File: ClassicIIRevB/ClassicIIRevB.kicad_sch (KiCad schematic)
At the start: 57 parts, among them J11 POWER/ANALOG, J15 BURN-IN

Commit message: Show smaller ROM footprints
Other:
- sheet Expansion Slot renamed Expansion Slot and Jumpers
- sheet System ROM renamed System ROM 128K & 256K
- added sheet System ROM 512K & 1M (rom2.kicad_sch)
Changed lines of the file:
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@@
 	(title_block
 		(title "Macintosh Classic II Revision B")
-		(date "2025-05-29")
+		(date "2025-05-31")
 		(company "Apple Computer")
 		(comment 1 "drawn by Bradley Bell")
@@
 	)
 	(sheet
-		(at 127 25.4)
+		(at 114.3 25.4)
 		(size 12.7 3.81)
 		(exclude_from_sim no)
@@
 		)
 		(property "Sheetname" "ADB & Battery"
-			(at 127 24.6884 0)
+			(at 114.3 24.6884 0)
 			(effects
 				(font
@@
 		)
 		(property "Sheetfile" "egret.kicad_sch"
-			(at 127 29.7946 0)
+			(at 114.3 29.7946 0)
 			(effects
 				(font
@@
 	)
 	(sheet
-		(at 203.2 35.56)
+		(at 139.7 45.72)
+		(size 12.7 3.81)
+		(exclude_from_sim no)
+		(in_bom yes)
+		(on_board yes)
+		(dnp no)
+		(fields_autoplaced yes)
+		(stroke
+			(width 0.1524)
+			(type solid)
+		)
+		(fill
+			(color 0 0 0 0.0000)
+		)
+		(property "Sheetname" "System ROM 512K & 1M"
+			(at 139.7 45.0084 0)
+			(effects
+				(font
+					(size 1.27 1.27)
+				)
+				(justify left bottom)
+			)
+		)
+		(property "Sheetfile" "rom2.kicad_sch"
+			(at 139.7 50.1146 0)
+			(effects
+				(font
+					(size 1.27 1.27)
+				)
+				(justify left top)
+			)
+		)
+		(instances
+			(project "ClassicIIRevB"
+				(path "/08c23af6-72f1-4a8f-a60c-b986fe71300f"
+					(page "7")
+				)
+			)
+		)
+	)
+	(sheet
+		(at 201.93 45.72)
 		(size 12.7 3.81)
 		(exclude_from_sim no)
@@
 		)
 		(property "Sheetname" "Floppy"
-			(at 203.2 34.8484 0)
+			(at 201.93 45.0084 0)
 			(effects
 				(font
@@
 		)
 		(property "Sheetfile" "floppy.kicad_sch"
-			(at 203.2 39.9546 0)
+			(at 201.93 50.1146 0)
 			(effects
 				(font
@@
 			(project "ClassicIIRevB"
 				(path "/08c23af6-72f1-4a8f-a60c-b986fe71300f"
-					(page "12")
+					(page "13")
 				)
 			)
@@
 	)
 	(sheet
-		(at 177.8 35.56)
+		(at 177.8 45.72)
 		(size 12.7 3.81)
 		(exclude_from_sim no)
@@
 		)
 		(property "Sheetname" "RAM Expansion"
-			(at 177.8 34.8484 0)
+			(at 177.8 45.0084 0)
 			(effects
 				(font
@@
 		)
 		(property "Sheetfile" "simm.kicad_sch"
-			(at 177.8 39.9546 0)
+			(at 177.8 50.1146 0)
 			(effects
 				(font
@@
 			(project "ClassicIIRevB"
 				(path "/08c23af6-72f1-4a8f-a60c-b986fe71300f"
-					(page "9")
+					(page "10")
 				)
 			)
@@
 	)
 	(sheet
-		(at 177.8 45.72)
+		(at 201.93 25.4)
 		(size 12.7 3.81)
 		(exclude_from_sim no)
@@
 		)
 		(property "Sheetname" "SCSI & Serial"
-			(at 177.8 45.0084 0)
+			(at 201.93 24.6884 0)
 			(effects
 				(font
@@
 		)
 		(property "Sheetfile" "scsi.kicad_sch"
-			(at 177.8 50.1146 0)
+			(at 201.93 29.7946 0)
 			(effects
 				(font
@@
 			(project "ClassicIIRevB"
 				(path "/08c23af6-72f1-4a8f-a60c-b986fe71300f"
-					(page "10")
+					(page "11")
 				)
 			)
@@
 	)
 	(sheet
-		(at 177.8 25.4)
+		(at 177.8 35.56)
 		(size 12.7 3.81)
 		(exclude_from_sim no)
@@
 		)
 		(property "Sheetname" "RAM"
-			(at 177.8 24.6884 0)
+			(at 177.8 34.8484 0)
 			(effects
 				(font
@@
 		)
 		(property "Sheetfile" "ram.kicad_sch"
-			(at 177.8 29.7946 0)
+			(at 177.8 39.9546 0)
 			(effects
 				(font
@@
 			(project "ClassicIIRevB"
 				(path "/08c23af6-72f1-4a8f-a60c-b986fe71300f"
-					(page "8")
+					(page "9")
 				)
 			)
@@
 	)
 	(sheet
-		(at 152.4 45.72)
+		(at 177.8 25.4)
 		(size 12.7 3.81)
 		(exclude_from_sim no)
@@
 		)
 		(property "Sheetname" "RAM Transceivers"
-			(at 152.4 45.0084 0)
+			(at 177.8 24.6884 0)
 			(effects
 				(font
@@
 		)
 		(property "Sheetfile" "xcvr.kicad_sch"
-			(at 152.4 50.1146 0)
+			(at 177.8 29.7946 0)
 			(effects
 				(font
@@
 			(project "ClassicIIRevB"
 				(path "/08c23af6-72f1-4a8f-a60c-b986fe71300f"
-					(page "7")
+					(page "8")
 				)
 			)
@@
 	)
 	(sheet
-		(at 127 45.72)
+		(at 114.3 45.72)
 		(size 12.7 3.81)
 		(exclude_from_sim no)
@@
 		)
 		(property "Sheetname" "EAGLE"
-			(at 127 45.0084 0)
+			(at 114.3 45.0084 0)
 			(effects
 				(font
@@
 		)
 		(property "Sheetfile" "eagle.kicad_sch"
-			(at 127 50.1146 0)
+			(at 114.3 50.1146 0)
 			(effects
 				(font
@@
 	)
 	(sheet
-		(at 152.4 35.56)
+		(at 139.7 25.4)
 		(size 12.7 3.81)
 		(exclude_from_sim no)
@@
 			(color 0 0 0 0.0000)
 		)
-		(property "Sheetname" "Expansion Slot"
-			(at 152.4 34.8484 0)
+		(property "Sheetname" "Expansion Slot and Jumpers"
+			(at 139.7 24.6884 0)
 			(effects
 				(font
@@
 		)
 		(property "Sheetfile" "romfpu.kicad_sch"
-			(at 152.4 39.9546 0)
+			(at 139.7 29.7946 0)
 			(effects
 				(font
@@
 			(project "ClassicIIRevB"
 				(path "/08c23af6-72f1-4a8f-a60c-b986fe71300f"
-					(page "6")
+					(page "5")
 				)
 			)
@@
 	)
 	(sheet
-		(at 203.2 45.72)
+		(at 228.6 25.4)
 		(size 12.7 3.81)
 		(exclude_from_sim no)
@@
 		)
 		(property "Sheetname" "Sound"
-			(at 203.2 45.0084 0)
+			(at 228.6 24.6884 0)
 			(effects
 				(font
@@
 		)
 		(property "Sheetfile" "sound.kicad_sch"
-			(at 203.2 50.1146 0)
+			(at 228.6 29.7946 0)
 			(effects
 				(font
@@
 			(project "ClassicIIRevB"
 				(path "/08c23af6-72f1-4a8f-a60c-b986fe71300f"
-					(page "13")
+					(page "14")
 				)
 			)
@@
 	)
 	(sheet
-		(at 127 35.56)
+		(at 114.3 35.56)
 		(size 12.7 3.81)
 		(exclude_from_sim no)
@@
 		)
 		(property "Sheetname" "CPU"
-			(at 127 34.8484 0)
+			(at 114.3 34.8484 0)
 			(effects
 				(font
@@
 		)
 		(property "Sheetfile" "cpu.kicad_sch"
-			(at 127 39.9546 0)
+			(at 114.3 39.9546 0)
 			(effects
 				(font
@@
 	)
 	(sheet
-		(at 203.2 25.4)
+		(at 201.93 35.56)
 		(size 12.7 3.81)
 		(exclude_from_sim no)
@@
 		)
 		(property "Sheetname" "Serial"
-			(at 203.2 24.638 0)
+			(at 201.93 34.798 0)
 			(effects
 				(font
@@
 		)
 		(property "Sheetfile" "serial.kicad_sch"
-			(at 203.2 29.718 0)
+			(at 201.93 39.878 0)
 			(effects
 				(font
@@
 			(project "ClassicIIRevB"
 				(path "/08c23af6-72f1-4a8f-a60c-b986fe71300f"
-					(page "11")
+					(page "12")
 				)
 			)
@@
 	)
 	(sheet
-		(at 228.6 25.4)
+		(at 228.6 35.56)
 		(size 12.7 3.81)
 		(exclude_from_sim no)
@@
 		)
 		(property "Sheetname" "DFAC"
-			(at 228.6 24.6884 0)
+			(at 228.6 34.8484 0)
 			(effects
 				(font
@@
 		)
 		(property "Sheetfile" "dfac.kicad_sch"
-			(at 228.6 29.7946 0)
+			(at 228.6 39.9546 0)
 			(effects
 				(font
@@
 			(project "ClassicIIRevB"
 				(path "/08c23af6-72f1-4a8f-a60c-b986fe71300f"
-					(page "14")
+					(page "15")
 				)
 			)
@@
 	)
 	(sheet
-		(at 152.4 25.4)
+		(at 139.7 35.56)
 		(size 12.7 3.81)
 		(exclude_from_sim no)
@@
 			(color 0 0 0 0.0000)
 		)
-		(property "Sheetname" "System ROM"
-			(at 152.4 24.6884 0)
+		(property "Sheetname" "System ROM 128K & 256K"
+			(at 139.7 34.8484 0)
 			(effects
 				(font
@@
 		)
 		(property "Sheetfile" "rom.kicad_sch"
-			(at 152.4 29.7946 0)
+			(at 139.7 39.9546 0)
 			(effects
 				(font
@@
 			(project "ClassicIIRevB"
 				(path "/08c23af6-72f1-4a8f-a60c-b986fe71300f"
-					(page "5")
+					(page "6")
 				)
 			)
@@
 			(project "ClassicIIRevB"
 				(path "/08c23af6-72f1-4a8f-a60c-b986fe71300f"
-					(page "15")
+					(page "16")
 				)
 			)

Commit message: improved footprints and silkscreens
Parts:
- FD1, FD6: footprint Fiducial:Fiducial_1mm_Mask3mm -> MyPackage:Fiducial_1mm_Mask3mm_square
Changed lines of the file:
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@@
 	(title_block
 		(title "Macintosh Classic II Revision B")
-		(date "2025-05-31")
+		(date "2025-06-04")
 		(company "Apple Computer")
 		(comment 1 "drawn by Bradley Bell")
@@
 			)
 		)
-		(property "Footprint" "Fiducial:Fiducial_1mm_Mask3mm"
+		(property "Footprint" "MyPackage:Fiducial_1mm_Mask3mm_square"
 			(at 147.32 200.66 0)
 			(effects
@@
 			)
 		)
-		(property "Footprint" "Fiducial:Fiducial_1mm_Mask3mm"
+		(property "Footprint" "MyPackage:Fiducial_1mm_Mask3mm_square"
 			(at 147.32 175.26 0)
 			(effects

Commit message: Switch to some "official" net names
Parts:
- added R83: 100, MyPackage:SMD_0805_2012Metric_Pad1.25x1.65mm, symbol Device:R_Small_US
- added TP186: ~, MyPackage:TestPoint_THTPad_D1.0mm_Drill0.5mm, symbol Connector:TestPoint
- F1: value Polyfuse_Small -> 1A
- L10, L2: value L_Ferrite_Small -> Ferrite
- L7: value L_Ferrite_Small -> FERRITE
- renumbered alt_G1 to ZG1
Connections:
- net BURN7 renamed BURNIN
- net OSC_VCC renamed G1_5V
- net PBL renamed PWM
- net SCSI_BSY renamed BSY
- net SPEAKER renamed SNDPOS
- net SYSCLOCKIN renamed 32MC
- net VIDEO renamed VIDOUTF
- net VIDOUTF: now also R83.2, TP186.1
- new net VIDOUT: R83.1
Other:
- moved on the sheet: C26, C31, C90, F1, J15, L10, L2, R76, R85, R93, R95

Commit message: update exports
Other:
- title: Macintosh Classic II Revision B -> Macintosh Classic II (Later Revision)
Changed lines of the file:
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@@
 	(paper "USLetter")
 	(title_block
-		(title "Macintosh Classic II Revision B")
-		(date "2025-06-04")
+		(title "Macintosh Classic II (Later Revision)")
+		(date "2025-06-16")
 		(company "Apple Computer")
 		(comment 1 "drawn by Bradley Bell")

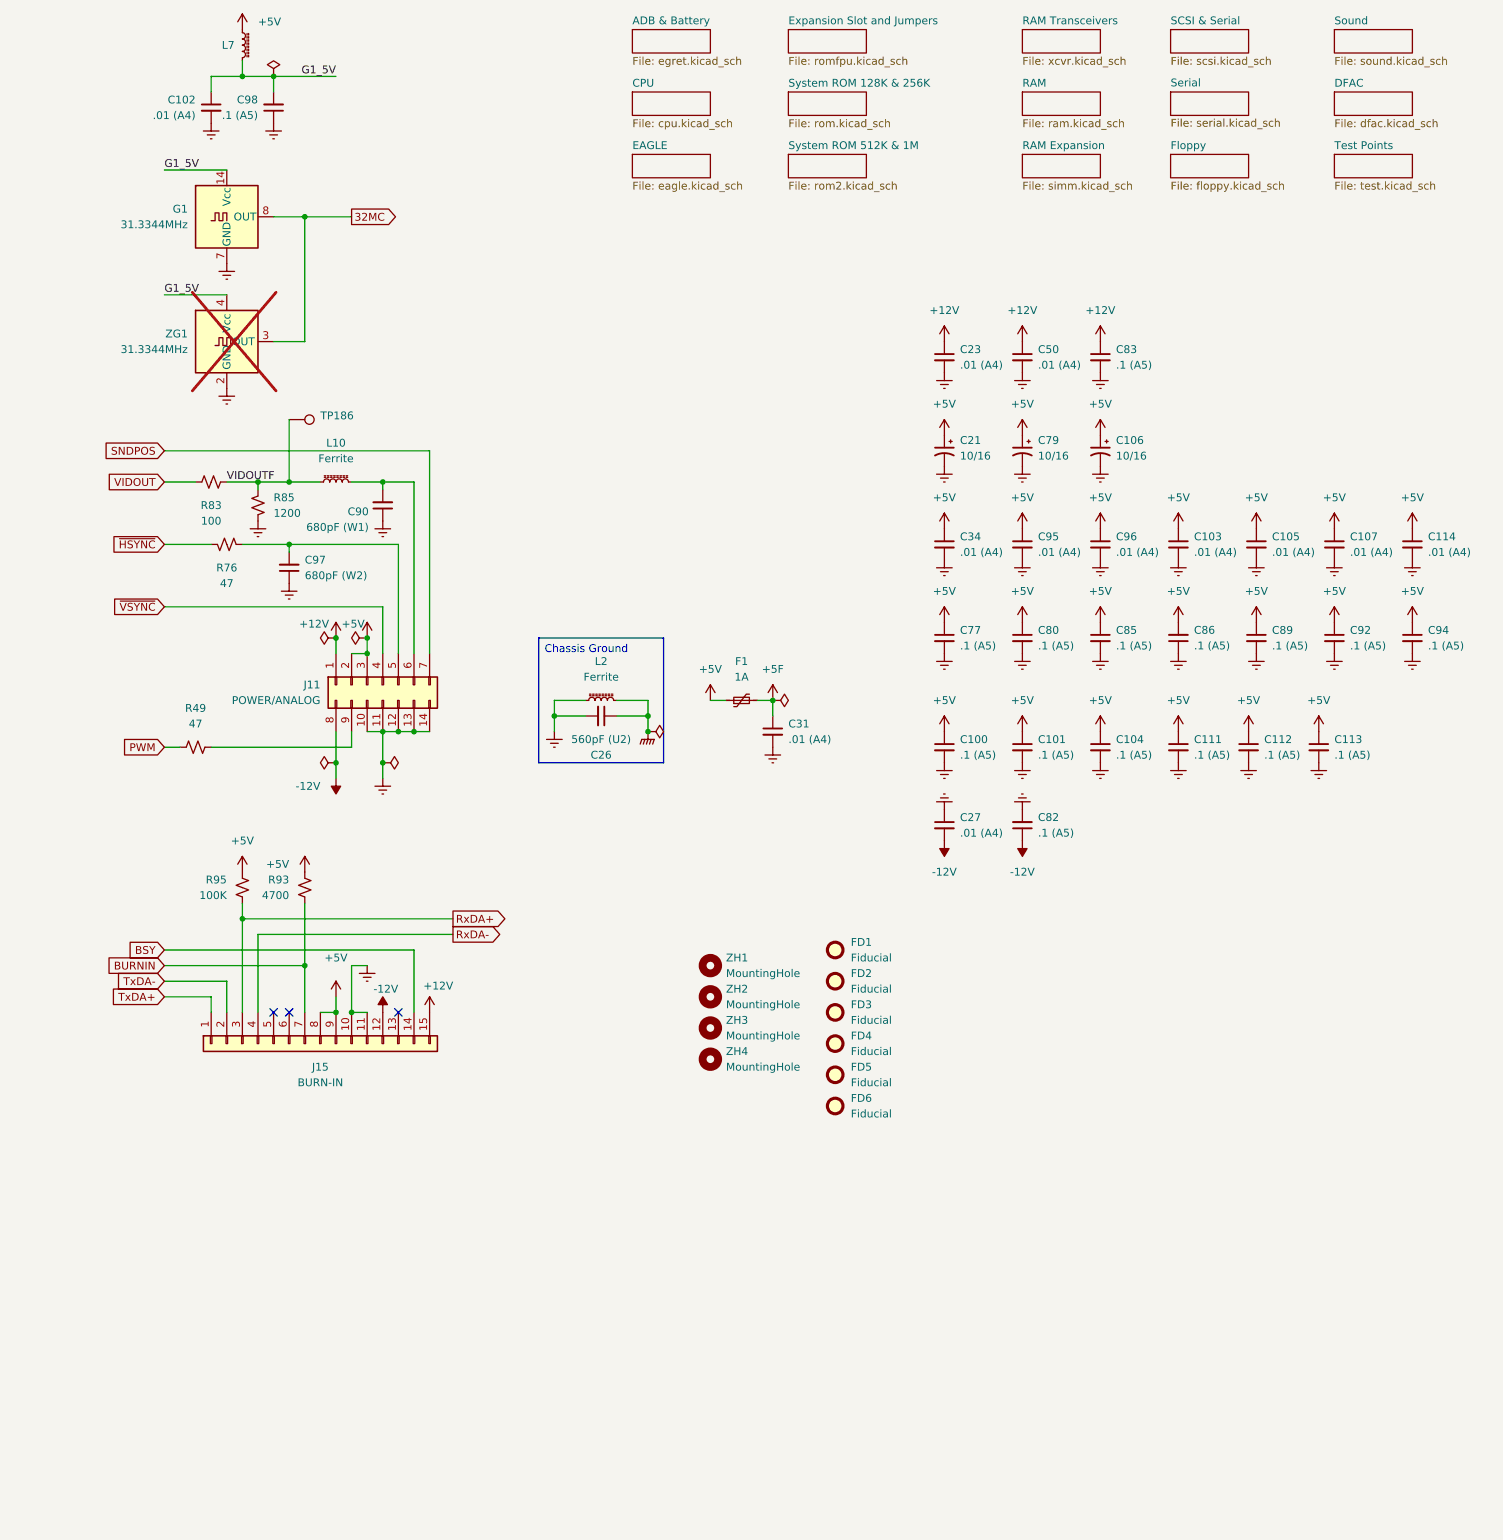
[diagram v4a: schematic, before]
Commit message: Corrections to SMDs, more improved footprints
The later revision board reproduction design is now complete.
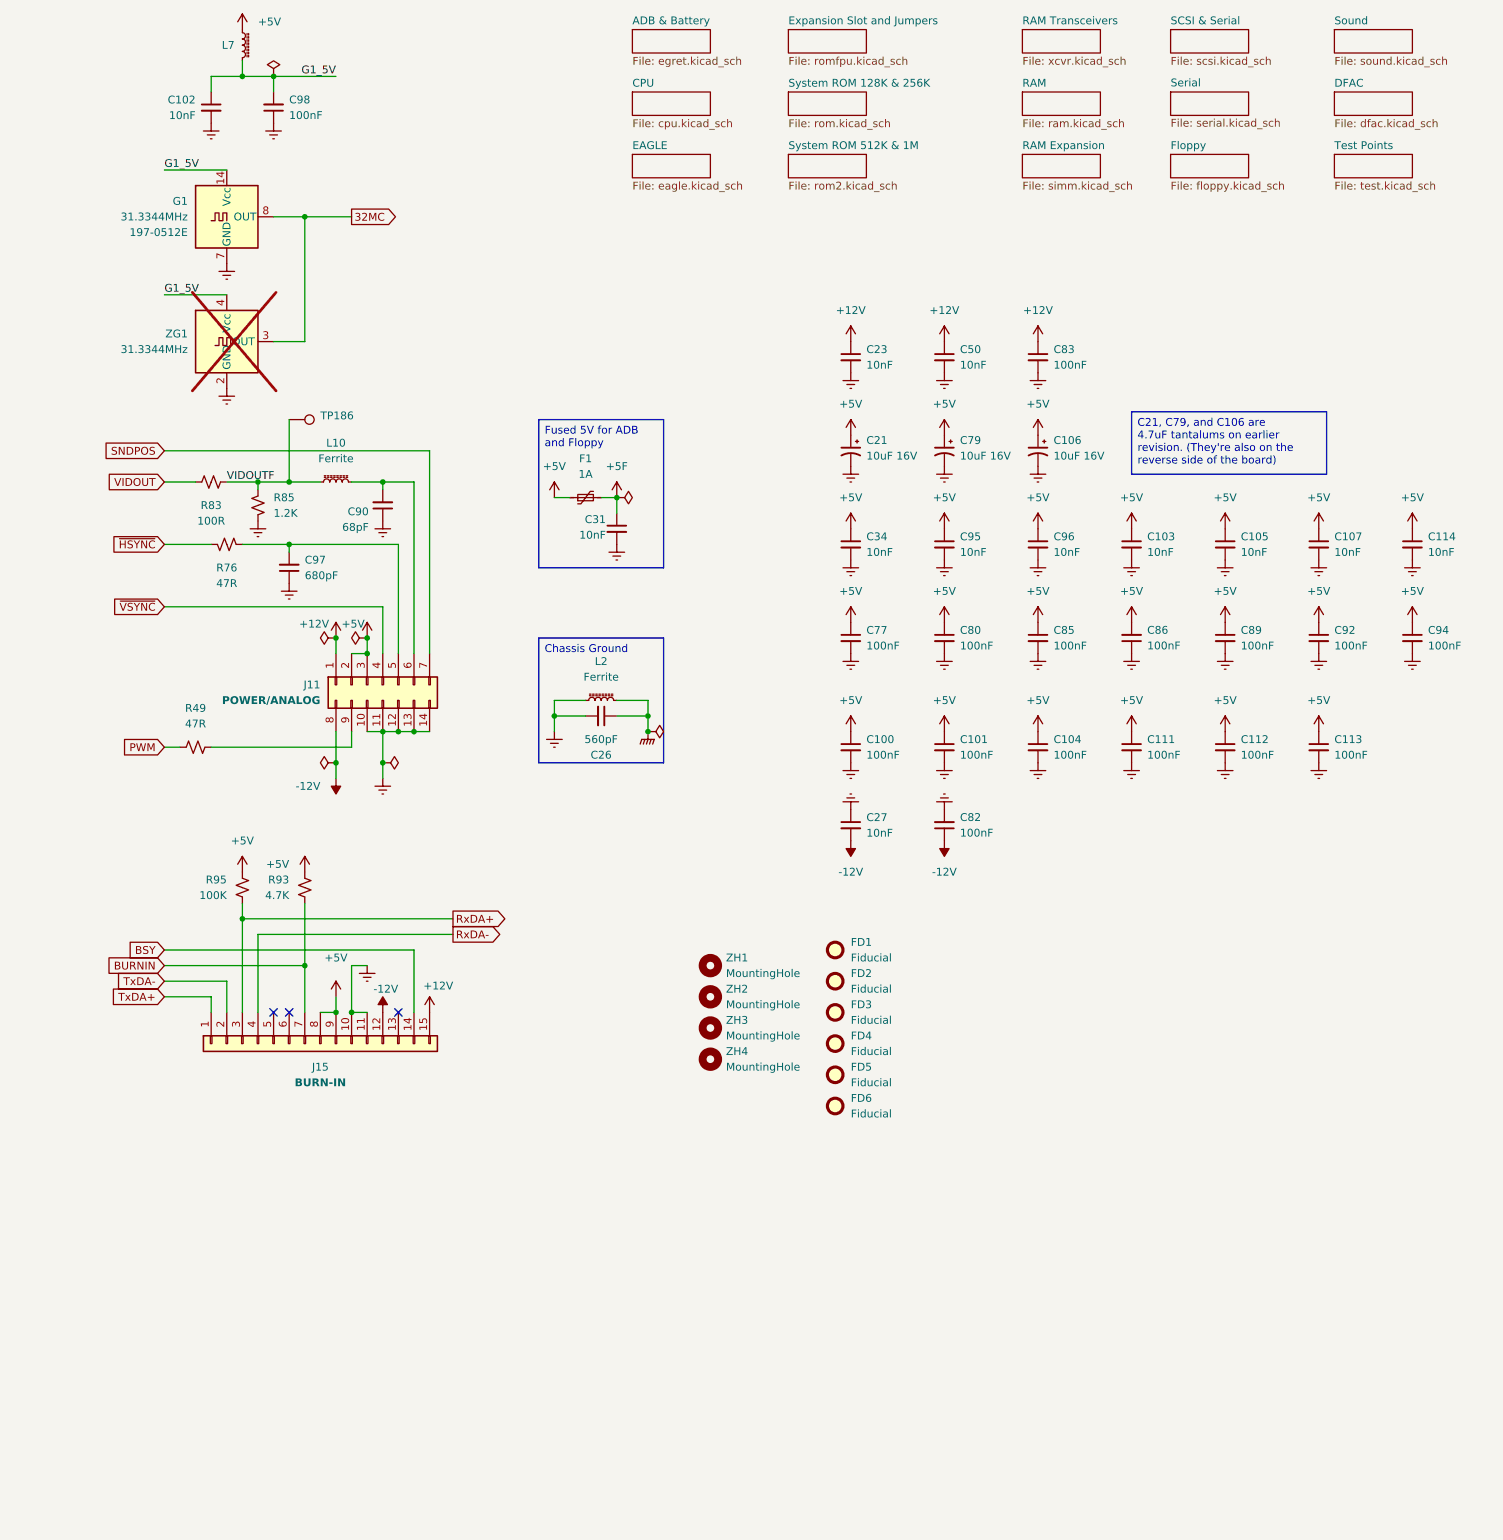
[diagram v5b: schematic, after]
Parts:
- C100, C101, C104, C111, C112, C113, C77, C80, C82, C83, C85, C86, C89, C92, C94, C98: value .1 (A5) -> 100nF
- C102, C103, C105, C107, C114, C23, C27, C31, C34, C50, C95, C96: value .01 (A4) -> 10nF
- C106, C79: value 10/16 -> 10uF 16V; Note (none) -> 4.7uF tant on earlier revision
- C21: value 10/16 -> 10uF 16V; Note (none) -> 4.7uF tant on early revision
- C26: value 560pF (U2) -> 560pF
- C90: value 680pF (W1) -> 68pF
- C97: value 680pF (W2) -> 680pF
- G1: footprint Oscillator:Oscillator_DIP-14 -> MyPackage:Oscillator_DIP-14; PartNum (none) -> 197-0512E
- J15, TP186: now left out of the parts list
- L7: value FERRITE -> Ferrite
- R49, R76: value 47 -> 47R
- R83: value 100 -> 100R
- R85: value 1200 -> 1.2K
- R93: value 4700 -> 4.7K
- ZG1: footprint Oscillator:Oscillator_SMD_Abracon_ABLNO -> MyPackage:Oscillator_SMD_Abracon_ABLNO
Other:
- moved on the sheet: C100, C101, C103, C104, C105, C106, C107, C111, C112, C21, C23, C27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

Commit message: Fix zones
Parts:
- ZH1, ZH2, ZH3, ZH4: footprint MountingHole:MountingHole_3.2mm_M3_ISO14580 -> MyPackage:MountingHole_3.2mm_M3_ISO14580
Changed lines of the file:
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@@
 	(title_block
 		(title "Macintosh Classic II (Later Revision)")
-		(date "2025-06-21")
+		(date "2025-06-23")
 		(company "Apple Computer")
 		(comment 1 "drawn by Bradley Bell")
@@
 			)
 		)
-		(property "Footprint" "MountingHole:MountingHole_3.2mm_M3_ISO14580"
+		(property "Footprint" "MyPackage:MountingHole_3.2mm_M3_ISO14580"
 			(at 127 177.8 0)
 			(effects
@@
 			)
 		)
-		(property "Footprint" "MountingHole:MountingHole_3.2mm_M3_ISO14580"
+		(property "Footprint" "MyPackage:MountingHole_3.2mm_M3_ISO14580"
 			(at 127 187.96 0)
 			(effects
@@
 			)
 		)
-		(property "Footprint" "MountingHole:MountingHole_3.2mm_M3_ISO14580"
+		(property "Footprint" "MyPackage:MountingHole_3.2mm_M3_ISO14580"
 			(at 127 182.88 0)
 			(effects
@@
 			)
 		)
-		(property "Footprint" "MountingHole:MountingHole_3.2mm_M3_ISO14580"
+		(property "Footprint" "MyPackage:MountingHole_3.2mm_M3_ISO14580"
 			(at 127 193.04 0)
 			(effects
